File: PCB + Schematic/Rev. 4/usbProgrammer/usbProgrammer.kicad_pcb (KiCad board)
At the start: 2 copper layers, 11.4 x 24 mm, 12 parts, among them J1 USBC, J2 USB, U1 Linear Step-Down

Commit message: Finish USB breakout
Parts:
- turned C2 to 90 degrees
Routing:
- net Net-(J1-CC1): track 2.99 -> 5.90 mm, vias 0 -> 2
- net D- Ext: track 19.3 -> 20.4 mm
- net USB: track 13.8 -> 14.6 mm
- net Net-(J1-SHIELD): track 23.8 -> 23.9 mm, vias 0 -> 2
- net Earth: vias 0 -> 13
- added copper zone on B.Cu, net Earth
- added copper zone on In1.Cu, net Earth
- added copper zone on In2.Cu, net Earth
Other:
- board size 11.4 x 24 mm -> 11.9 x 24 mm
- copper layers 2 -> 4

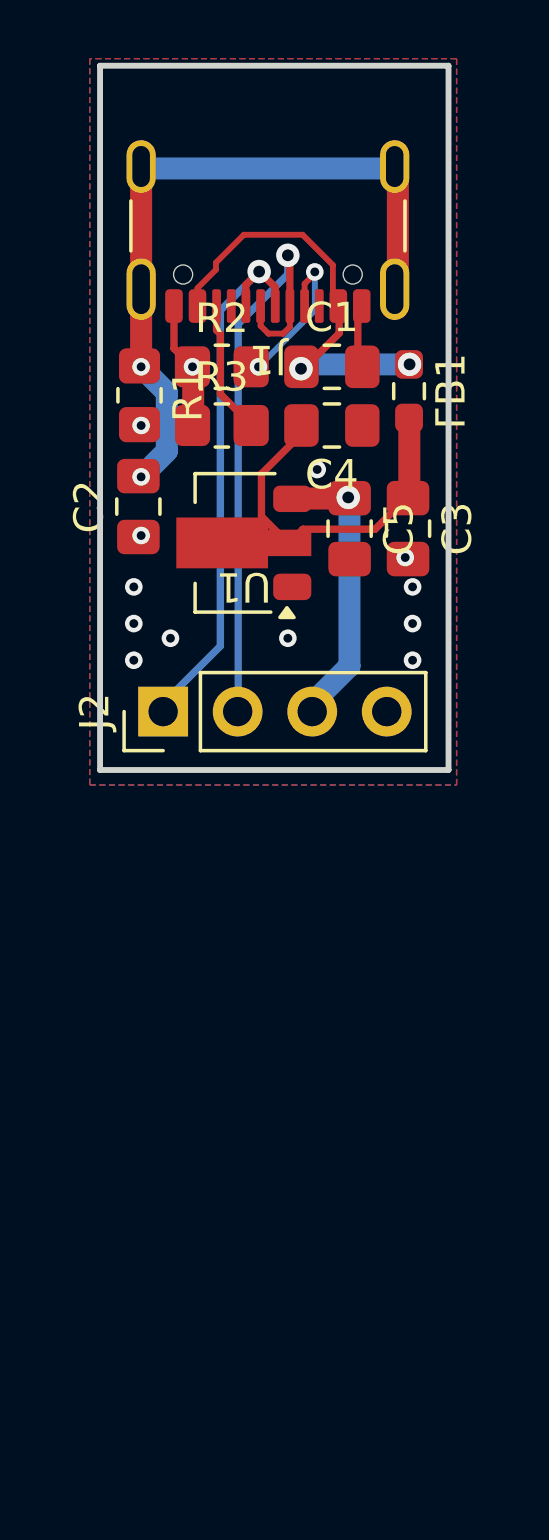
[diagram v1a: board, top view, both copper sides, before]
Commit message: USB, 3D models, Reference Designators
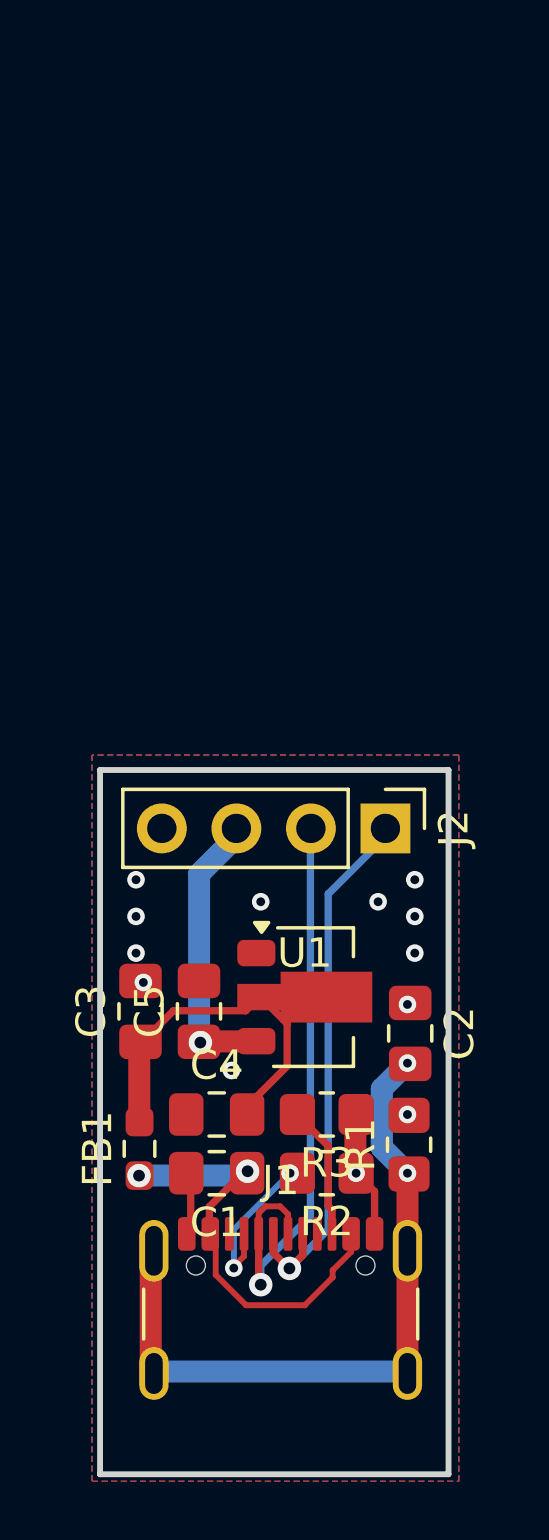
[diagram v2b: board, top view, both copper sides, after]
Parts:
- moved J1 39.0 mm to (137.3, 111.0), turned to 0 degrees
- moved C1 27.8 mm to (135.1, 105.2), turned to 180 degrees
- moved R2 27.7 mm to (138.8, 105.2), turned to 180 degrees
- moved FB1 27.4 mm to (132.4, 104.4), turned to 90 degrees
- moved R1 27.1 mm to (141.6, 104.3), turned to 90 degrees
- moved C4 23.8 mm to (135.1, 103.2), turned to 0 degrees
- moved R3 23.8 mm to (138.8, 103.2), turned to 180 degrees
- moved C2 20.2 mm to (141.7, 100.5), turned to -90 degrees
- moved C3 18.8 mm to (132.5, 99.7), turned to 90 degrees
- moved C5 17.2 mm to (134.5, 99.7), turned to 90 degrees
- moved U1 15.6 mm to (138.1, 99.2), turned to 0 degrees
- moved J2 8.56 mm to (140.8, 93.5), turned to -90 degrees
